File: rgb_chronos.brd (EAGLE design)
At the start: 160 x 100 mm, 0 parts

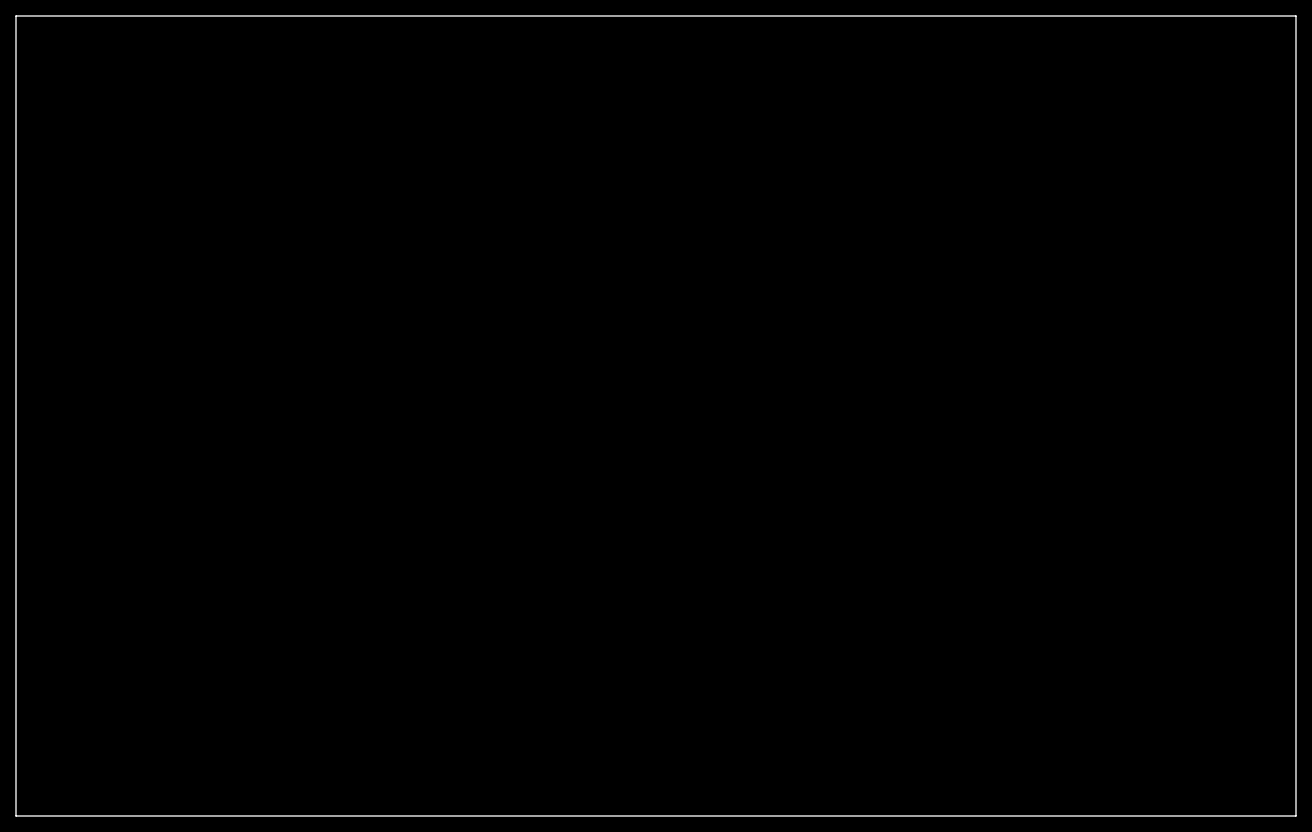
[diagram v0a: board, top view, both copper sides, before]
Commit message: LEDs added to dircuit and board
Multiplexing implemented
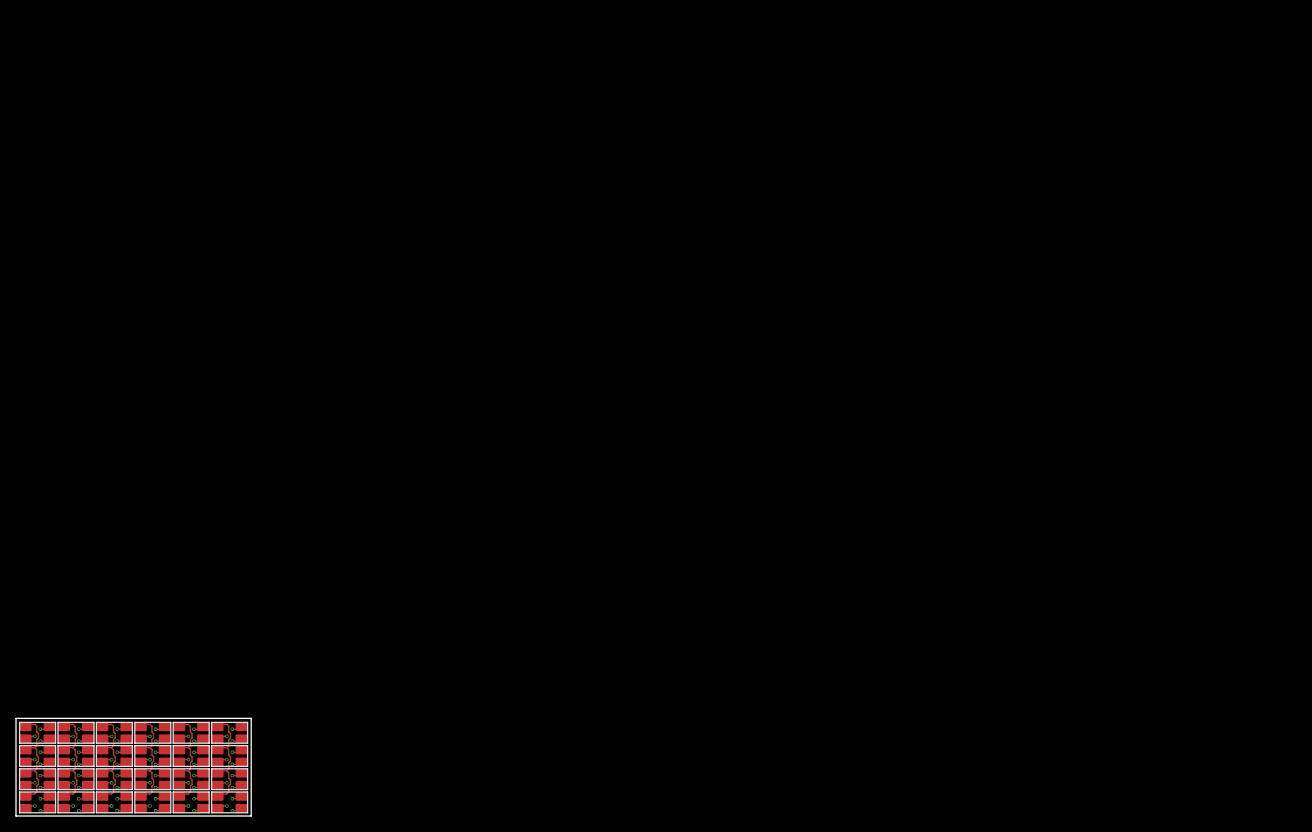
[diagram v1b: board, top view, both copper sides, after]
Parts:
- added U$1, U$10, U$11, U$12, U$13, U$14, U$15, U$16, U$17, U$18, U$19, U$2, U$20, U$21, U$22, U$23, U$24, U$3, U$4, U$5, U$6, U$7, U$8, U$9: LED3_ARGB, pmg-library:PLCC4-LED
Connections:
- new net N$1: U$1.P$1, U$2.P$1, U$3.P$1, U$4.P$1
- new net N$10: U$12.P$4, U$16.P$4, U$20.P$4, U$24.P$4, U$4.P$4, U$8.P$4
- new net N$11: U$11.P$3, U$15.P$3, U$19.P$3, U$23.P$3, U$3.P$3, U$7.P$3
- new net N$12: U$11.P$2, U$15.P$2, U$19.P$2, U$23.P$2, U$3.P$2, U$7.P$2
- new net N$13: U$10.P$4, U$14.P$4, U$18.P$4, U$2.P$4, U$22.P$4, U$6.P$4
- new net N$14: U$10.P$3, U$14.P$3, U$18.P$3, U$2.P$3, U$22.P$3, U$6.P$3
- new net N$15: U$10.P$2, U$14.P$2, U$18.P$2, U$2.P$2, U$22.P$2, U$6.P$2
- new net N$16: U$1.P$4, U$13.P$4, U$17.P$4, U$21.P$4, U$5.P$4, U$9.P$4
- new net N$17: U$1.P$3, U$13.P$3, U$17.P$3, U$21.P$3, U$5.P$3, U$9.P$3
- new net N$18: U$1.P$2, U$13.P$2, U$17.P$2, U$21.P$2, U$5.P$2, U$9.P$2
- new net N$2: U$21.P$1, U$22.P$1, U$23.P$1, U$24.P$1
- new net N$3: U$17.P$1, U$18.P$1, U$19.P$1, U$20.P$1
- new net N$4: U$13.P$1, U$14.P$1, U$15.P$1, U$16.P$1
- new net N$5: U$10.P$1, U$11.P$1, U$12.P$1, U$9.P$1
- new net N$6: U$5.P$1, U$6.P$1, U$7.P$1, U$8.P$1
- new net N$7: U$11.P$4, U$15.P$4, U$19.P$4, U$23.P$4, U$3.P$4, U$7.P$4
- new net N$8: U$12.P$2, U$16.P$2, U$20.P$2, U$24.P$2, U$4.P$2, U$8.P$2
- new net N$9: U$12.P$3, U$16.P$3, U$20.P$3, U$24.P$3, U$4.P$3, U$8.P$3
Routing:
- net N$6: track 0.00 -> 14.9 mm
- net N$3: track 0.00 -> 14.9 mm
- net N$4: track 0.00 -> 14.9 mm
- net N$1: track 0.00 -> 14.9 mm
- net N$5: track 0.00 -> 14.9 mm
- net N$2: track 0.00 -> 14.9 mm
- net N$13: track 0.00 -> 7.65 mm, vias 0 -> 6
- net N$9: track 0.00 -> 7.65 mm, vias 0 -> 6
- net N$8: track 0.00 -> 7.65 mm, vias 0 -> 6
- net N$16: track 0.00 -> 7.65 mm, vias 0 -> 6
- net N$18: track 0.00 -> 7.65 mm, vias 0 -> 6
- net N$14: track 0.00 -> 7.65 mm, vias 0 -> 6
- net N$7: track 0.00 -> 7.65 mm, vias 0 -> 6
- net N$17: track 0.00 -> 7.65 mm, vias 0 -> 6
- net N$10: track 0.00 -> 7.65 mm, vias 0 -> 6
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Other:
- board size 160 x 100 mm -> 29.4 x 12.2 mm

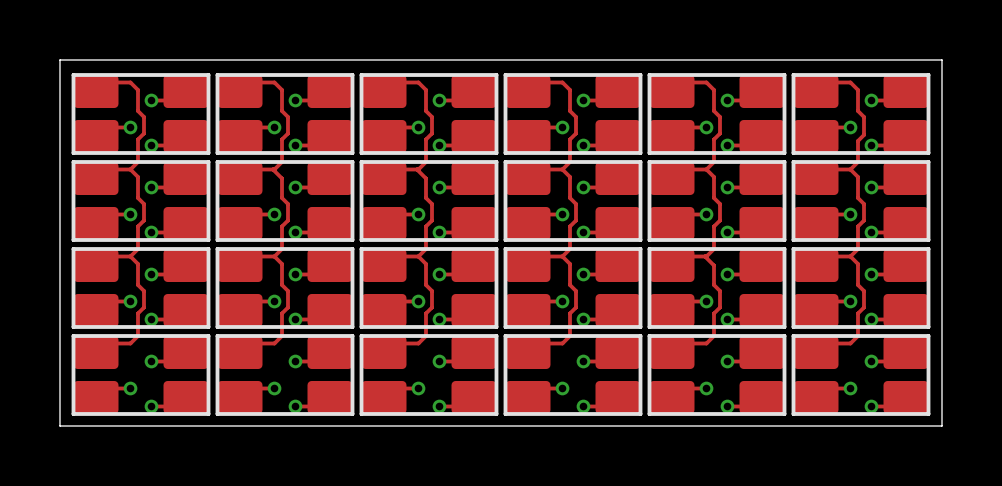
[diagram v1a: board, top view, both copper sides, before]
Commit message: Display self-routed
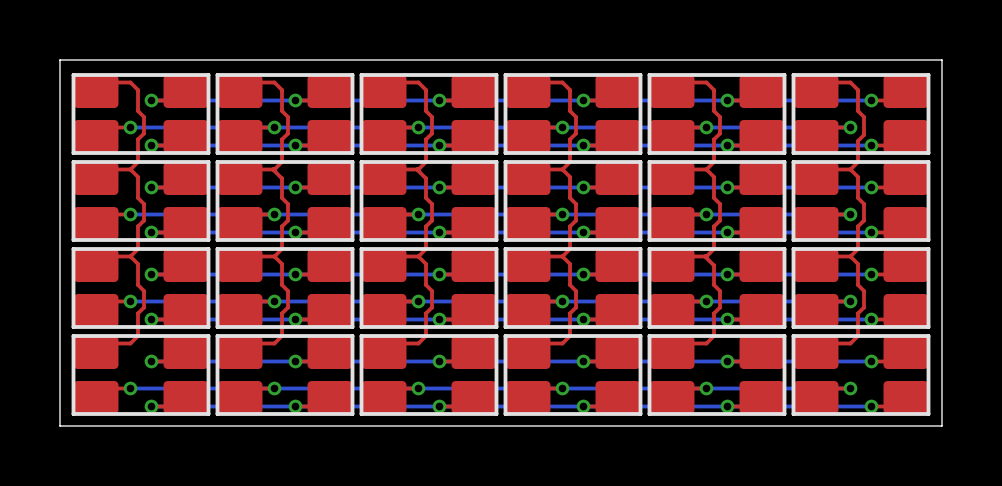
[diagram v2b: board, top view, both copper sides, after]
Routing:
- net N$17: track 7.65 -> 31.6 mm
- net N$16: track 7.65 -> 31.6 mm
- net N$9: track 7.65 -> 31.6 mm
- net N$8: track 7.65 -> 31.6 mm
- net N$7: track 7.65 -> 31.6 mm
- net N$18: track 7.65 -> 31.6 mm
- net N$14: track 7.65 -> 31.6 mm
- net N$13: track 7.65 -> 31.6 mm
- net N$10: track 7.65 -> 31.6 mm
- net N$15: track 7.65 -> 31.6 mm
- net N$12: track 7.65 -> 31.6 mm
- net N$11: track 7.65 -> 31.6 mm
